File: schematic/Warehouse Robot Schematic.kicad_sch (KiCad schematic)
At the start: 29 parts, among them J1 Conn_01x15_Pin, J10 Conn_01x03_Pin, J11 Conn_01x03_Pin, J12 Conn_01x02, J13 Conn_01x03_Pin, J2 Conn_01x15_Pin, J3 Conn_01x02, J4 Conn_01x02, J5 Conn_01x02, J6 Conn_01x02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

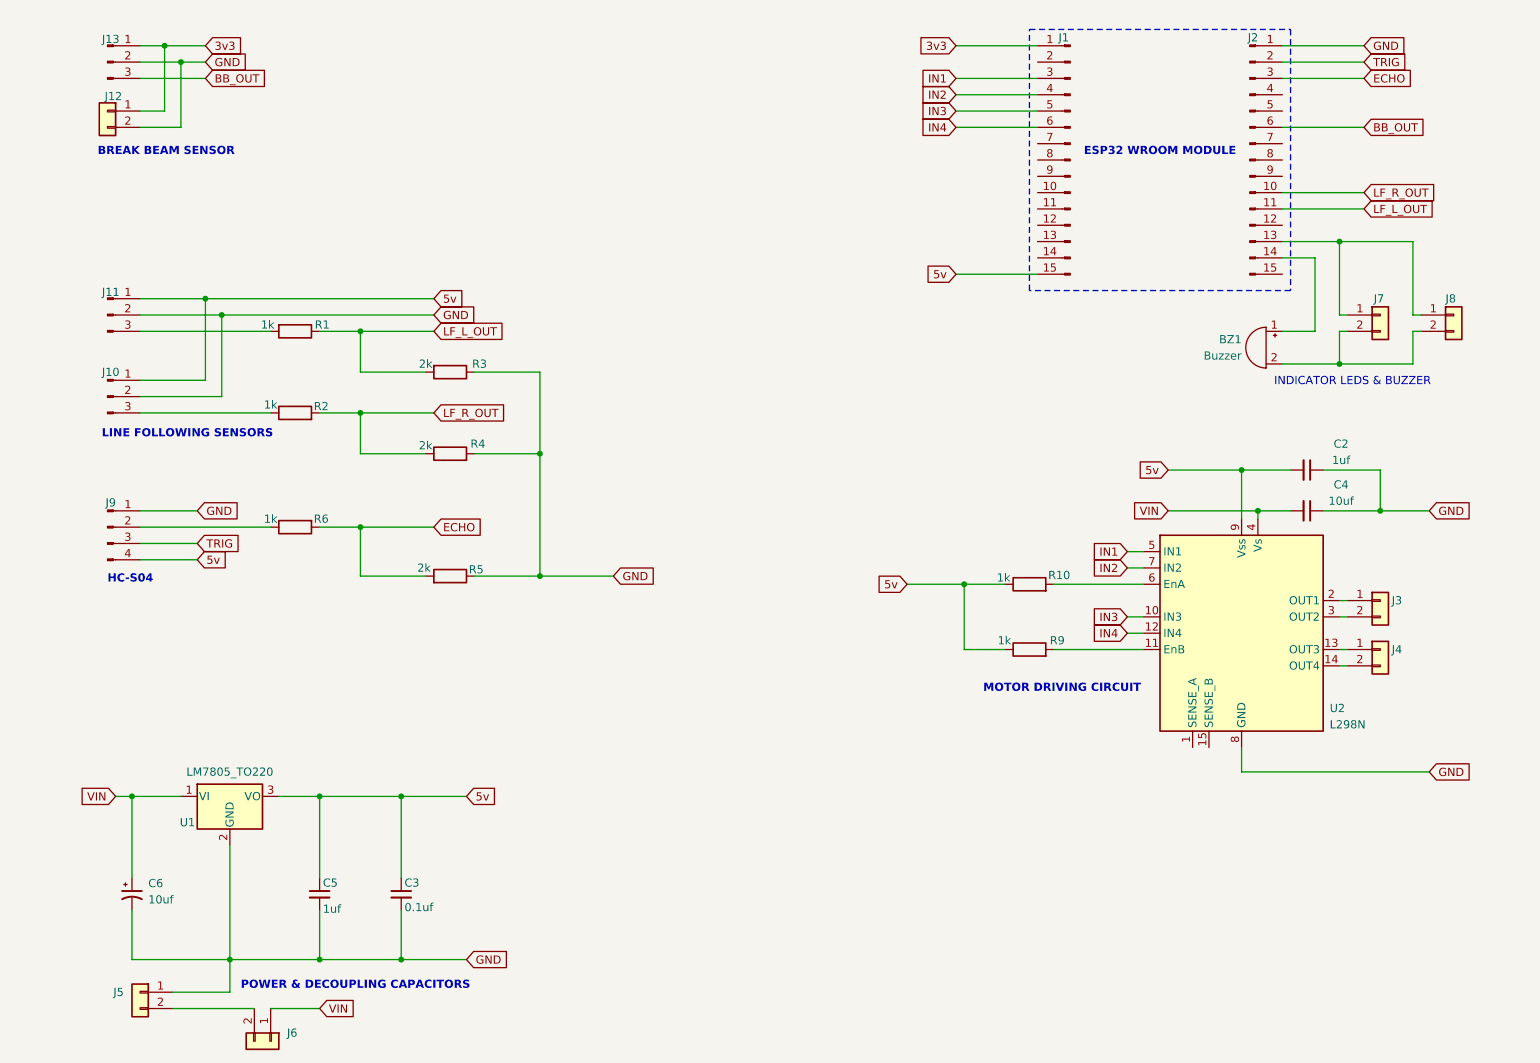
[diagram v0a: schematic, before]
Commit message: updated schematic with test points
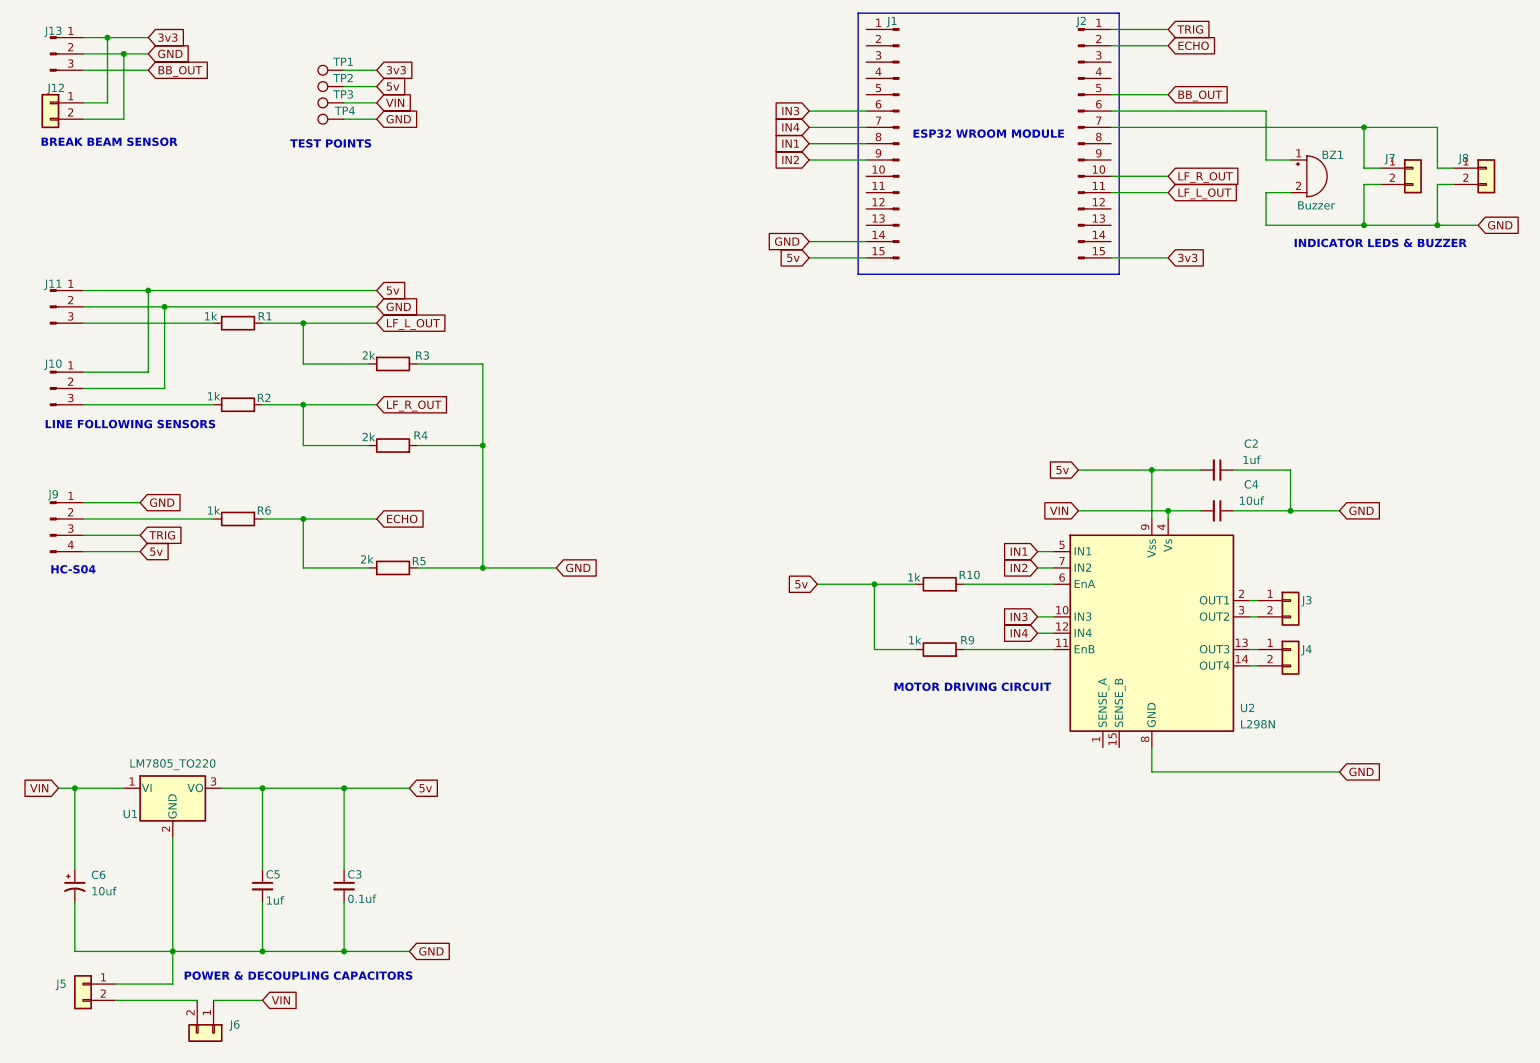
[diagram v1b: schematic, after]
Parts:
- added TP1, TP2, TP3, TP4: TestPoint, TestPoint:TestPoint_Loop_D3.50mm_Drill1.4mm_Beaded, symbol Connector:TestPoint
- C2: footprint Capacitor_THT:C_Axial_L3.8mm_D2.6mm_P7.50mm_Horizontal -> Capacitor_THT:C_Rect_L4.6mm_W3.0mm_P2.50mm_MKS02_FKP02
- C3, C4, C5: footprint (none) -> Capacitor_THT:C_Rect_L4.6mm_W3.0mm_P2.50mm_MKS02_FKP02
- C6: footprint (none) -> Capacitor_THT:C_Radial_D6.3mm_H5.0mm_P2.50mm
- J1: footprint Connector_Samtec_HPM_THT:Samtec_HPM-15-01-x-S_Straight_1x15_Pitch5.08mm -> Connector_PinSocket_2.54mm:PinSocket_1x15_P2.54mm_Vertical
- J10: footprint Connector_JST:JST_EH_S3B-EH_1x03_P2.50mm_Horizontal -> Connector_JST:JST_XH_B3B-XH-AM_1x03_P2.50mm_Vertical
- J11: footprint (none) -> Connector_JST:JST_XH_B3B-XH-AM_1x03_P2.50mm_Vertical
- J12, J6, J7: footprint (none) -> Connector_JST:JST_XH_B2B-XH-AM_1x02_P2.50mm_Vertical
- J13: footprint Connector_JST:JST_EH_B3B-EH-A_1x03_P2.50mm_Vertical -> Connector_JST:JST_XH_B3B-XH-AM_1x03_P2.50mm_Vertical
- J2: footprint (none) -> Connector_PinSocket_2.54mm:PinSocket_1x15_P2.54mm_Vertical
- J4: footprint (none) -> Connector_JST:JST_EH_S2B-EH_1x02_P2.50mm_Horizontal
- J5, J8: footprint Connector:JWT_A3963_1x02_P3.96mm_Vertical -> Connector_JST:JST_XH_B2B-XH-AM_1x02_P2.50mm_Vertical
- J9: footprint Connector_JST:JST_EH_B4B-EH-A_1x04_P2.50mm_Vertical -> Connector_JST:JST_XH_B4B-XH-AM_1x04_P2.50mm_Vertical
- R1: footprint Resistor_THT:R_Bare_Metal_Element_L12.4mm_W4.8mm_P11.40mm -> Resistor_THT:R_Axial_DIN0207_L6.3mm_D2.5mm_P10.16mm_Horizontal
- R10, R2, R3, R4, R5, R6, R9: footprint (none) -> Resistor_THT:R_Axial_DIN0207_L6.3mm_D2.5mm_P10.16mm_Horizontal
- U2: footprint Package_TO_SOT_THT:TO-220-15_P2.54x5.08mm_StaggerOdd_Lead4.58mm_Vertical -> Package_TO_SOT_THT:TO-220F-15_P2.54x5.08mm_StaggerOdd_Lead5.08mm_Vertical
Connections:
- net 3v3: now also J2.15 (Pin_15), TP1.1; no longer J1.1 (Pin_1)
- net 5v: now also TP2.1
- net BB_OUT: now also J2.5 (Pin_5); no longer J2.6 (Pin_6)
- net ECHO: now also J2.2 (Pin_2); no longer J2.3 (Pin_3)
- net GND: now also BZ1.2 (-), J1.14 (Pin_14), J7.2 (Pin_2), J8.2 (Pin_2), TP4.1; no longer J2.1 (Pin_1)
- net IN1: now also J1.8 (Pin_8); no longer J1.3 (Pin_3)
- net IN2: now also J1.9 (Pin_9); no longer J1.4 (Pin_4)
- net IN3: now also J1.6 (Pin_6); no longer J1.5 (Pin_5)
- net IN4: now also J1.7 (Pin_7); no longer J1.6 (Pin_6)
- net TRIG: now also J2.1 (Pin_1); no longer J2.2 (Pin_2)
- net VIN: now also TP3.1
- net at J7.1 (Pin_1), J8.1 (Pin_1): now also J2.7 (Pin_7); no longer J2.13 (Pin_13)
- net at BZ1.1 (+): now also J2.6 (Pin_6); no longer J2.14 (Pin_14)
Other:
- note added: "TEST POINTS"
- moved on the sheet: BZ1, C2, C3, C4, C5, C6, J1, J10, J11, J12, J13, J2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
